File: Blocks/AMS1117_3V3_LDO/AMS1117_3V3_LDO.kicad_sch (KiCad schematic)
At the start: 5 parts, among them U4 AMS1117-3.3

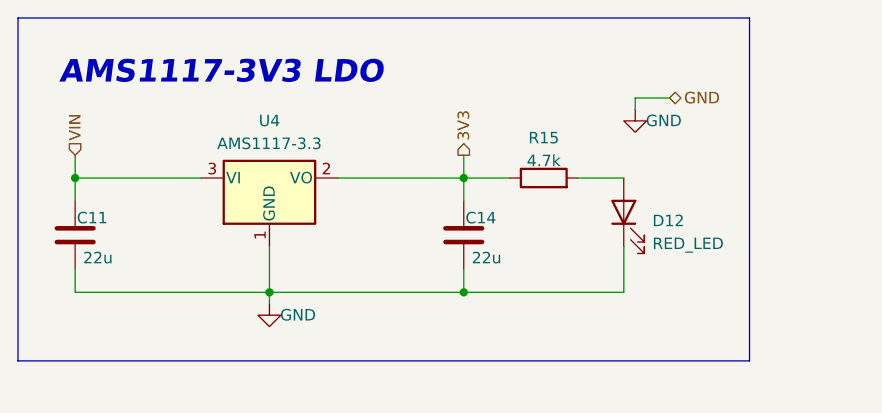
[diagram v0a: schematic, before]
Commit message: Added ideal LDO block
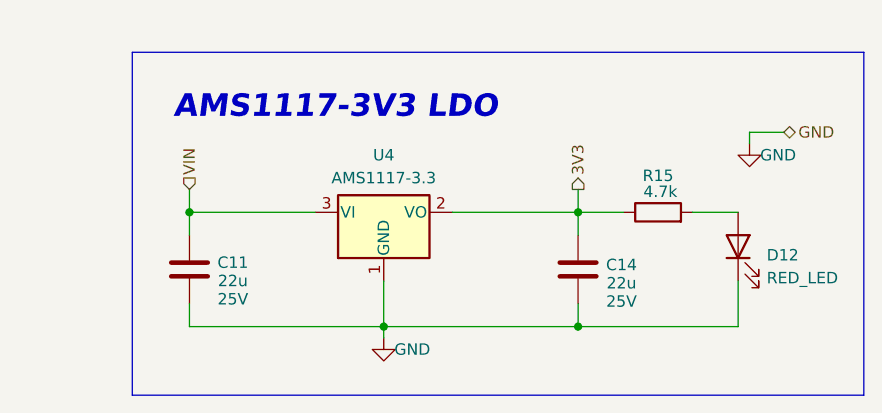
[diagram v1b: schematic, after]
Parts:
- C11, C14: MPN (none) -> CL31A226KAHNNNE; Voltage (none) -> 25V
- D12: LCSC Part # C2286 -> C6784992; MPN (none) -> 150060SS75000
- R15: MPN (none) -> 0603WAF4701T5E
- U4: MPN C6186 -> AMS1117-3.3
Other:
- moved on the sheet: C11, C14, D12, R15, U4
